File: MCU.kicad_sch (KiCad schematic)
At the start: 13 parts

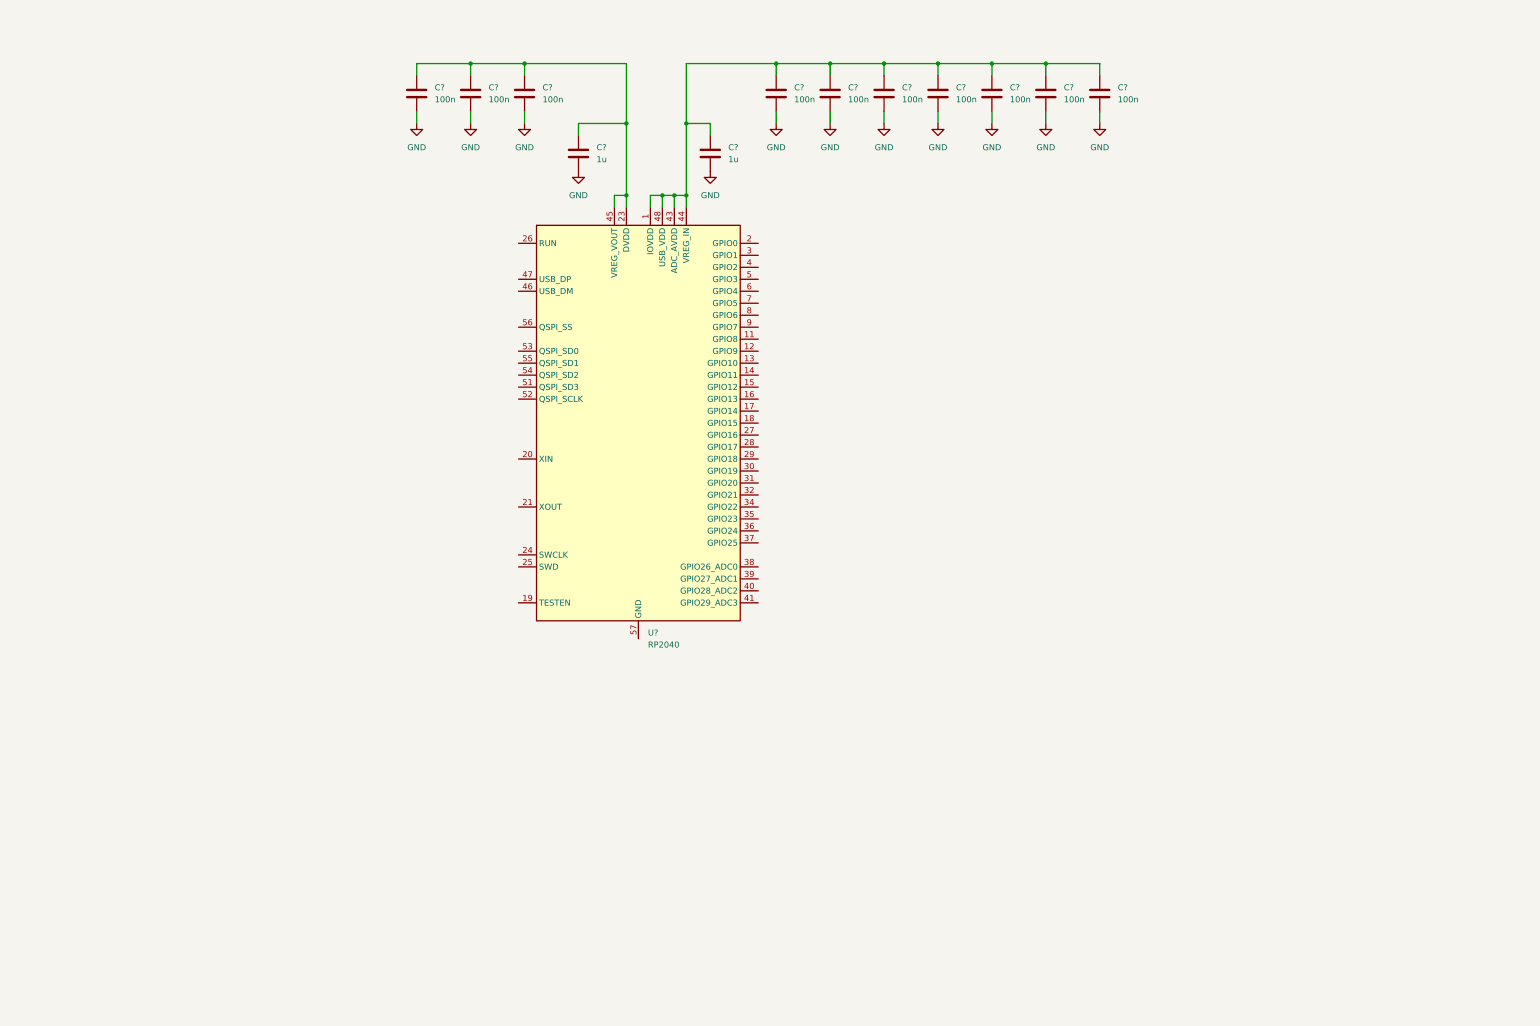
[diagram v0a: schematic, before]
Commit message: finished telemetry
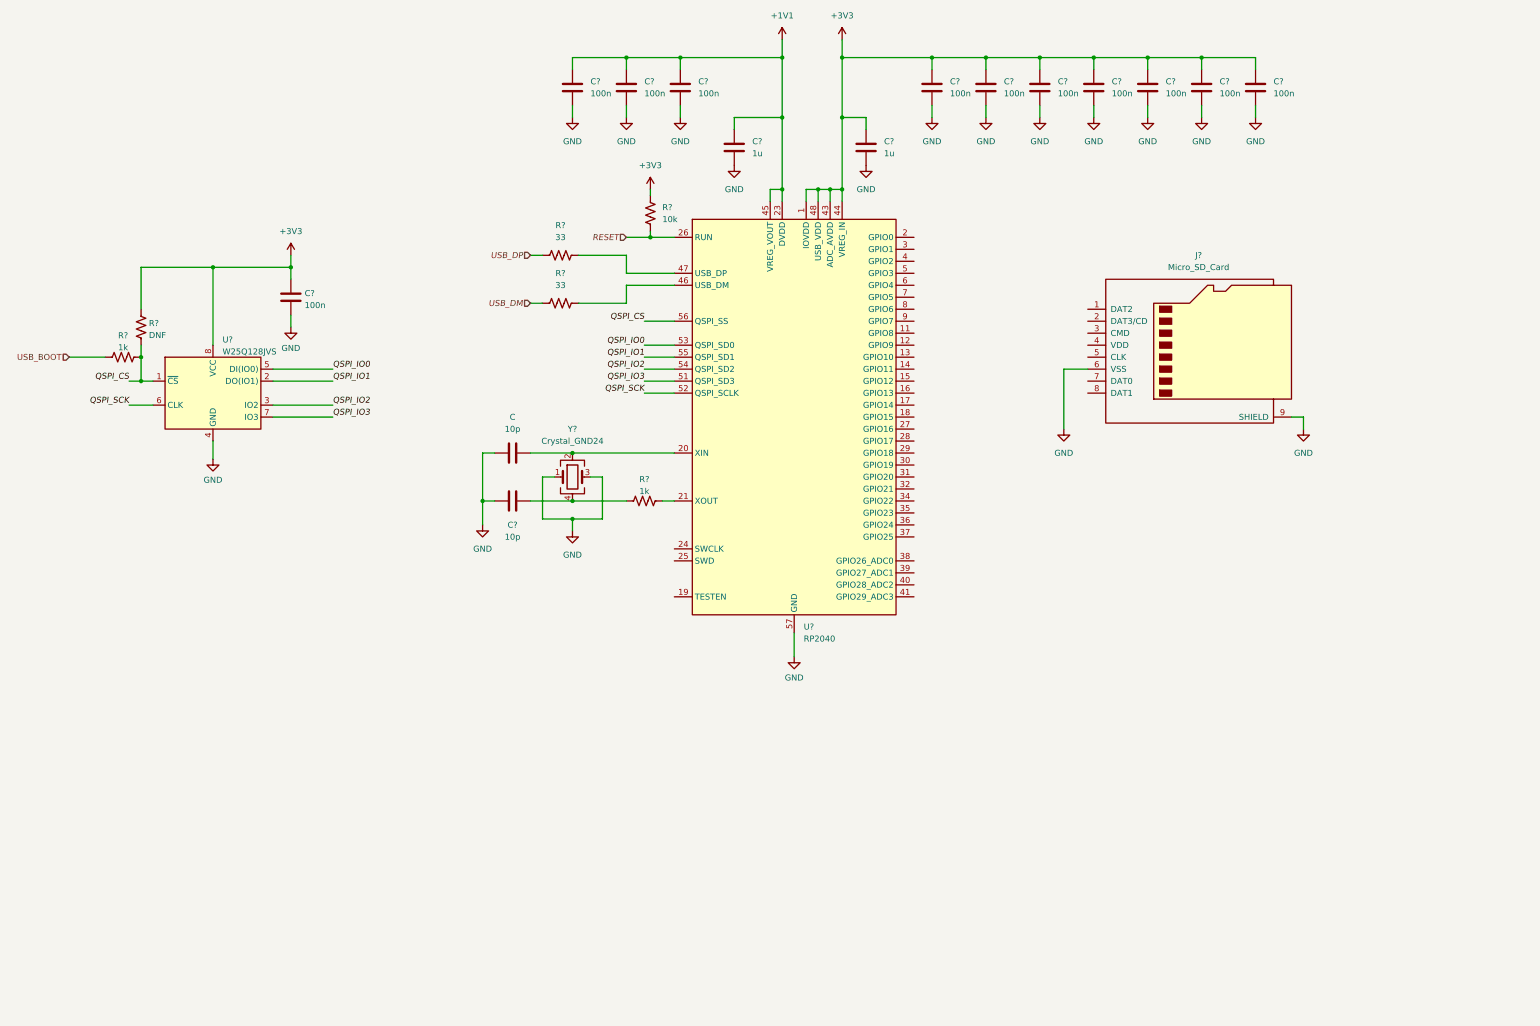
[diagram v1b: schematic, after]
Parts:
- added C, C?: 10p, Capacitor_SMD:C_0402_1005Metric, symbol Device:C
- added C?: 100n, Capacitor_SMD:C_0402_1005Metric, symbol Device:C
- added J?: Micro_SD_Card, symbol Connector:Micro_SD_Card
- added R?: DNF, Resistor_SMD:R_0805_2012Metric, symbol Device:R_US
- added R?: 10k, Resistor_SMD:R_0402_1005Metric, symbol Device:R_US
- added R? (x2): 1k, Resistor_SMD:R_0402_1005Metric, symbol Device:R_US
- added R? (x2): 33, Resistor_SMD:R_0402_1005Metric, symbol Device:R_US
- added U?: W25Q128JVS, Package_SO:SOIC-8_5.23x5.23mm_P1.27mm, symbol Memory_Flash:W25Q128JVS
- added Y?: Crystal_GND24, symbol Device:Crystal_GND24
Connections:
- net GND: now also U?.57 (GND), C.1, C?.1, C?.2, J?.6 (VSS), J?.9 (SHIELD), U?.4 (GND), Y?.1, Y?.3
- net +3V3: now reaches C?.1, C?.1, C?.1, C?.1, C?.1, C?.1, C?.1, C?.1, U?.1 (IOVDD), U?.10 (IOVDD), U?.22 (IOVDD), U?.33 (IOVDD), U?.42 (IOVDD), U?.43 (ADC_AVDD), U?.44 (VREG_IN), U?.48 (USB_VDD), U?.49 (IOVDD)
- net +3V3: now also C?.1, R?.1, R?.2, U?.8 (VCC)
- net +1V1: now reaches C?.1, C?.1, C?.1, C?.1, U?.23 (DVDD), U?.45 (VREG_VOUT), U?.50 (DVDD)
- net at U?.20 (XIN): now also C.2, Y?.2
- net at U?.21 (XOUT): now also R?.2
- net RESET: now reaches U?.26 (RUN)
- net RESET: now also R?.1
- net at U?.46 (USB_DM): now also R?.1
- net at U?.47 (USB_DP): now also R?.1
- net QSPI_IO3: now reaches U?.51 (QSPI_SD3)
- net QSPI_IO3: now also U?.7 (IO3)
- net QSPI_SCK: now reaches U?.52 (QSPI_SCLK)
- net QSPI_SCK: now also U?.6 (CLK)
- net QSPI_IO0: now reaches U?.53 (QSPI_SD0)
- net QSPI_IO0: now also U?.5 (DI(IO0))
- net QSPI_IO2: now reaches U?.54 (QSPI_SD2)
- net QSPI_IO2: now also U?.3 (IO2)
- net QSPI_IO1: now reaches U?.55 (QSPI_SD1)
- net QSPI_IO1: now also U?.2 (DO(IO1))
- net QSPI_CS: now reaches U?.56 (QSPI_SS)
- net QSPI_CS: now also R?.2, R?.2, U?.1 (~{CS})
- new net: C?.2, R?.1, Y?.4
- new net USB_BOOT: R?.1
- new net USB_DM: R?.2
- new net USB_DP: R?.2
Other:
- moved on the sheet: C?, U?

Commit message: Finished Snesors
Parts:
- removed J?: Micro_SD_Card, symbol Connector:Micro_SD_Card
- added J?: Micro_SD_Card_Det, Connector_Card:microSD_HC_Hirose_DM3AT-SF-PEJM5, symbol Connector:Micro_SD_Card_Det
- added R?: 10k, Resistor_SMD:R_0402_1005Metric, symbol Device:R_US
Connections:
- net +3V3: now also J?.4 (VDD), R?.1
- net GND: now also J?.11 (SHIELD), J?.6 (VSS), J?.9 (DET_B)
- net SPI1_SDI: now reaches U?.15 (GPIO12)
- net SD_CS: now reaches U?.16 (GPIO13)
- net SPI1_SCK: now reaches U?.17 (GPIO14)
- net SPI1_SDO: now reaches U?.18 (GPIO15)
- new net: J?.10 (DET_A), R?.2
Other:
- moved on the sheet: C, C?, R?, U?, Y?

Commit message: started connecting board
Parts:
- added TP: SPI1_SDO, TestPoint:TestPoint_THTPad_1.0x1.0mm_Drill0.5mm, symbol Connector:TestPoint
- added TP?: SPI1_SCK, TestPoint:TestPoint_THTPad_1.0x1.0mm_Drill0.5mm, symbol Connector:TestPoint
- added TP?: SD_CS, TestPoint:TestPoint_THTPad_1.0x1.0mm_Drill0.5mm, symbol Connector:TestPoint
- added TP?: SPI1_SDI, TestPoint:TestPoint_THTPad_1.0x1.0mm_Drill0.5mm, symbol Connector:TestPoint
- R?: footprint Resistor_SMD:R_0402_1005Metric -> Resistor_SMD:R_0805_2012Metric
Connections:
- net SD_CS: now also J?.2 (DAT3/CD), TP?.1
- net SPI1_SCK: now also J?.5 (CLK), TP?.1
- net SPI1_SDI: now also J?.7 (DAT0), TP?.1
- net SPI1_SDO: now also J?.3 (CMD), TP.1
- net SD_D2: now reaches J?.1 (DAT2)
- net ~{SD_DET}: now reaches J?.10 (DET_A), R?.2
- net SD_D1: now reaches J?.8 (DAT1)
- net GPIO8: now reaches U?.11 (GPIO8)
- net GPIO9: now reaches U?.12 (GPIO9)
- net GPIO10: now reaches U?.13 (GPIO10)
- net GPIO11: now reaches U?.14 (GPIO11)
- net UART0_TX: now reaches U?.2 (GPIO0)
- net SPI0_SDI: now reaches U?.27 (GPIO16)
- net I2C0_SCL: now reaches U?.28 (GPIO17)
- net SPI0_SCK: now reaches U?.29 (GPIO18)
- net UART0_RX: now reaches U?.3 (GPIO1)
- net SPI0_SDO: now reaches U?.30 (GPIO19)
- net I2C0_SDA: now reaches U?.31 (GPIO20)
- net GPIO21: now reaches U?.32 (GPIO21)
- net GPIO22: now reaches U?.34 (GPIO22)
- net GPIO23: now reaches U?.35 (GPIO23)
- net GPIO24: now reaches U?.36 (GPIO24)
- net GPIO25: now reaches U?.37 (GPIO25)
- net A0: now reaches U?.38 (GPIO26_ADC0)
- net A1: now reaches U?.39 (GPIO27_ADC1)
- net GPIO2: now reaches U?.4 (GPIO2)
- net A2: now reaches U?.40 (GPIO28_ADC2)
- net A3: now reaches U?.41 (GPIO29_ADC3)
- net GPIO3: now reaches U?.5 (GPIO3)
- net GPIO4: now reaches U?.6 (GPIO4)
- net GPIO5: now reaches U?.7 (GPIO5)
- net GPIO6: now reaches U?.8 (GPIO6)
- net GPIO7: now reaches U?.9 (GPIO7)
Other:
- moved on the sheet: J?, R?

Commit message: finished routing
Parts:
- Y201: renamed from Y?; footprint (none) -> Crystal:Crystal_SMD_3225-4Pin_3.2x2.5mm
- gave numbers to parts that had none: 27
- renumbered C to C201, TP to TP202
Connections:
- net GPIO11 is gone; now on net ~{SD_DET}: U201.14 (GPIO11)
- net GND: now also U201.19 (TESTEN)
- net GPIO10: no longer names the net of U201.13 (GPIO10)
